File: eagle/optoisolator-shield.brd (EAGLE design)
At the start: 101.6 x 53.3 mm, 51 parts, among them Q1 MMBT2222ALT3G, Q2 MMBT2222ALT3G, Q3 MMBT2222ALT3G, Q4 MMBT2222ALT3G, Q5 MMBT2222ALT3G, Q6 MMBT2222ALT3G, U1 ILD213T, U2 ILD213T, U3 ILD213T

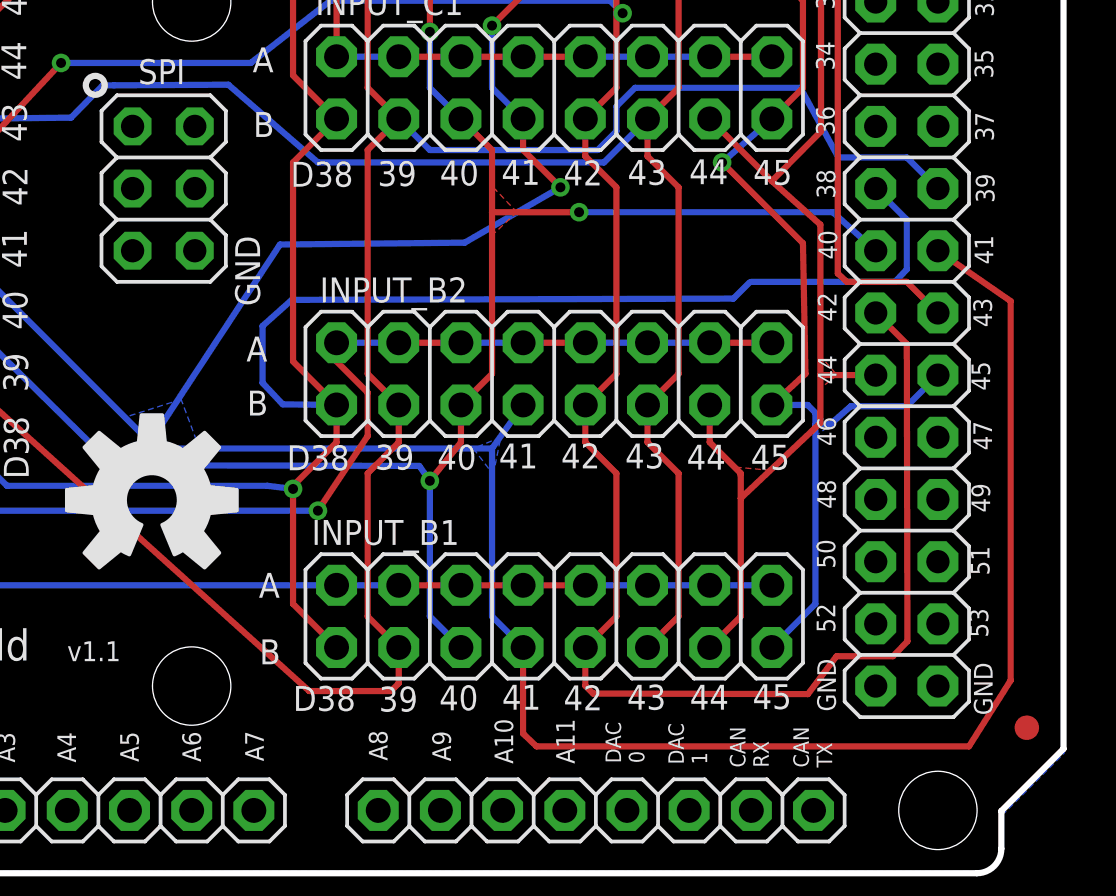
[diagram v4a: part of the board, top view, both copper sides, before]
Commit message: improved trace clearance and copper pour
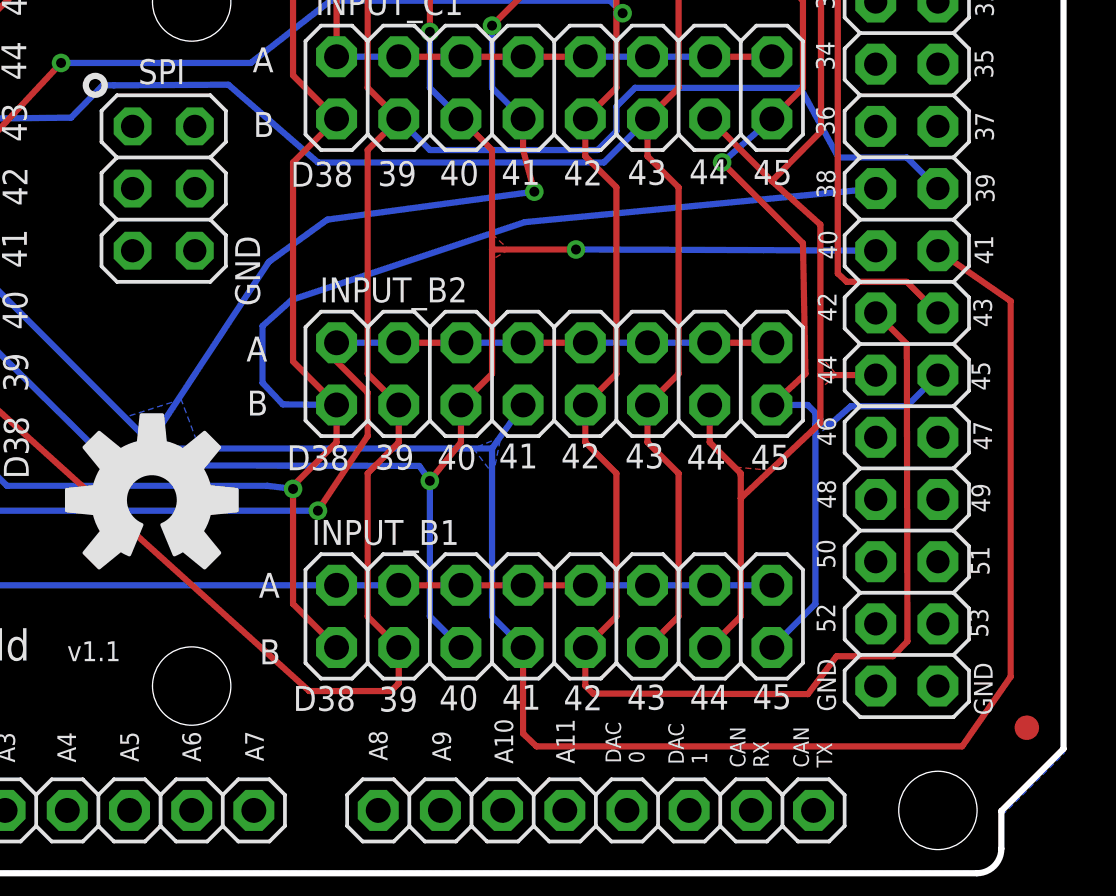
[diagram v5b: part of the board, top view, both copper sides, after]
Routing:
- net D38: track 98.5 -> 93.5 mm
- net D41: track 127.2 -> 125.2 mm
- net D40: track 83.9 -> 83.3 mm
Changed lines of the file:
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@@
 <wire x1="71.9582" y1="17.5768" x2="70.1802" y2="15.7988" width="0.254" layer="1"/>
 <wire x1="71.9582" y1="19.1008" x2="71.9582" y2="17.5768" width="0.254" layer="1"/>
-<wire x1="70.1294" y1="23.3934" x2="88.1634" y2="23.4442" width="0.254" layer="16"/>
 <wire x1="68.9356" y1="22.3266" x2="70.1294" y2="23.3934" width="0.254" layer="16"/>
 <wire x1="71.9582" y1="19.1008" x2="69.7611" y2="19.1262" width="0.254" layer="16"/>
@@
 <wire x1="71.9582" y1="19.1008" x2="70.1802" y2="20.8788" width="0.254" layer="1"/>
 <via x="70.1802" y="15.6718" extent="1-16" drill="0.4064"/>
-<wire x1="88.1634" y1="23.4442" x2="88.8238" y2="24.1046" width="0.254" layer="16"/>
-<wire x1="95.25" y1="26.67" x2="93.98" y2="27.94" width="0.254" layer="16"/>
-<wire x1="95.25" y1="24.638" x2="95.25" y2="26.67" width="0.254" layer="16"/>
-<wire x1="94.7674" y1="24.13" x2="95.25" y2="24.638" width="0.254" layer="16"/>
-<wire x1="88.9" y1="24.13" x2="94.7674" y2="24.13" width="0.254" layer="16"/>
-<wire x1="88.9" y1="24.13" x2="88.8238" y2="24.1046" width="0.1524" layer="16"/>
+<wire x1="93.98" y1="27.94" x2="79.6544" y2="26.5684" width="0.254" layer="16"/>
+<wire x1="79.6544" y1="26.5684" x2="70.1294" y2="23.3934" width="0.254" layer="16"/>
 </signal>
 <signal name="D45">
@@
 <wire x1="79.5782" y1="35.8648" x2="78.3082" y2="34.5948" width="0.254" layer="1"/>
 <wire x1="79.5782" y1="41.4528" x2="79.5782" y2="35.8648" width="0.254" layer="1"/>
-<wire x1="79.5782" y1="29.5148" x2="81.1022" y2="27.9908" width="0.254" layer="1"/>
+<wire x1="79.5782" y1="29.5148" x2="80.0354" y2="27.813" width="0.254" layer="1"/>
 <wire x1="79.5782" y1="30.7848" x2="79.5782" y2="29.5148" width="0.254" layer="1"/>
 <wire x1="48.8442" y1="26.9748" x2="47.5742" y2="25.7048" width="0.254" layer="16"/>
@@
 <wire x1="64.3382" y1="17.5768" x2="56.2102" y2="25.7048" width="0.254" layer="16"/>
 <wire x1="78.3082" y1="17.3228" x2="64.5922" y2="17.3228" width="0.254" layer="16"/>
-<wire x1="77.1906" y1="25.7302" x2="81.1022" y2="27.9908" width="0.254" layer="16"/>
-<wire x1="69.6468" y1="25.654" x2="77.1906" y2="25.7302" width="0.254" layer="16"/>
-<wire x1="64.3382" y1="17.5768" x2="69.6468" y2="25.654" width="0.254" layer="16"/>
+<wire x1="71.5772" y1="26.67" x2="80.0354" y2="27.813" width="0.254" layer="16"/>
+<wire x1="69.1896" y1="24.9428" x2="71.5772" y2="26.67" width="0.254" layer="16"/>
+<wire x1="64.3382" y1="17.5768" x2="69.1896" y2="24.9428" width="0.254" layer="16"/>
 <via x="78.3082" y="34.5948" extent="1-16" drill="0.4064"/>
-<via x="81.1022" y="27.9908" extent="1-16" drill="0.4064"/>
+<via x="80.0354" y="27.813" extent="1-16" drill="0.4064"/>
 <polygon width="0.0254" layer="16">
 <vertex x="65.6082" y="19.3294"/>
@@
 </polygon>
 <wire x1="99.4918" y1="23.3426" x2="96.52" y2="25.4" width="0.254" layer="1"/>
-<wire x1="99.4918" y1="7.8486" x2="99.4918" y2="23.3426" width="0.254" layer="1"/>
-<wire x1="97.79" y1="5.1562" x2="99.4918" y2="7.8486" width="0.254" layer="1"/>
+<wire x1="99.4918" y1="8.001" x2="99.4918" y2="23.3426" width="0.254" layer="1"/>
+<wire x1="97.5106" y1="5.1562" x2="99.4918" y2="8.001" width="0.254" layer="1"/>
 <wire x1="79.5782" y1="5.6769" x2="80.1243" y2="5.1562" width="0.254" layer="1"/>
-<wire x1="80.1243" y1="5.1562" x2="97.79" y2="5.1562" width="0.254" layer="1"/>
+<wire x1="80.1243" y1="5.1562" x2="97.5106" y2="5.1562" width="0.254" layer="1"/>
 <wire x1="79.5782" y1="5.6769" x2="79.5782" y2="9.1948" width="0.254" layer="1"/>
 </signal>
@@
 <wire x1="77.0382" y1="19.1008" x2="77.0382" y2="17.5768" width="0.254" layer="1"/>
 <wire x1="78.3082" y1="29.5148" x2="77.0382" y2="30.7848" width="0.254" layer="1"/>
-<wire x1="78.3082" y1="20.3708" x2="78.3082" y2="26.9748" width="0.254" layer="1"/>
-<wire x1="78.3082" y1="26.9748" x2="78.3082" y2="29.5148" width="0.254" layer="1"/>
+<wire x1="78.3082" y1="20.3708" x2="78.3082" y2="25.4508" width="0.254" layer="1"/>
+<wire x1="78.3082" y1="25.4508" x2="78.3082" y2="29.5148" width="0.254" layer="1"/>
 <wire x1="77.0382" y1="19.1008" x2="78.3082" y2="20.3708" width="0.254" layer="1"/>
 <wire x1="75.7682" y1="40.1828" x2="77.0382" y2="41.4528" width="0.254" layer="1"/>
 <wire x1="75.7682" y1="34.3408" x2="75.7682" y2="40.1828" width="0.254" layer="1"/>
 <wire x1="77.0382" y1="30.7848" x2="75.7682" y2="32.0548" width="0.254" layer="16"/>
-<wire x1="78.3082" y1="26.9748" x2="81.8642" y2="26.9748" width="0.254" layer="1"/>
+<wire x1="78.3082" y1="25.4508" x2="81.7372" y2="25.4508" width="0.254" layer="1"/>
 <wire x1="62.8142" y1="16.637" x2="56.2102" y2="23.1648" width="0.254" layer="16"/>
 <wire x1="75.3364" y1="16.6116" x2="62.8142" y2="16.637" width="0.254" layer="16"/>
@@
 <via x="75.7682" y="16.002" extent="1-16" drill="0.4064"/>
 <via x="75.7682" y="34.3408" extent="1-16" drill="0.4064"/>
-<via x="81.8642" y="26.9748" extent="1-16" drill="0.4064"/>
+<via x="81.7372" y="25.4508" extent="1-16" drill="0.4064"/>
+<wire x1="89.408" y1="25.4254" x2="93.98" y2="25.4" width="0.254" layer="16"/>
+<wire x1="89.408" y1="25.4254" x2="81.7372" y2="25.4508" width="0.254" layer="16"/>
+<wire x1="75.7682" y1="32.0548" x2="75.7682" y2="34.3408" width="0.254" layer="16"/>
 <polygon width="0.0254" layer="1">
-<vertex x="78.359" y="27.9908"/>
-<vertex x="79.3242" y="26.9748"/>
-<vertex x="78.2574" y="25.9842"/>
-</polygon>
-<wire x1="92.2274" y1="26.9748" x2="93.98" y2="25.4" width="0.254" layer="16"/>
-<wire x1="92.2274" y1="26.9748" x2="81.8642" y2="26.9748" width="0.254" layer="16"/>
-<wire x1="75.7682" y1="32.0548" x2="75.7682" y2="34.3408" width="0.254" layer="16"/>
+<vertex x="78.3082" y="26.0858"/>
+<vertex x="78.994" y="25.4508"/>
+<vertex x="78.2828" y="25.019"/>
+</polygon>
 </signal>
 <signal name="D39">

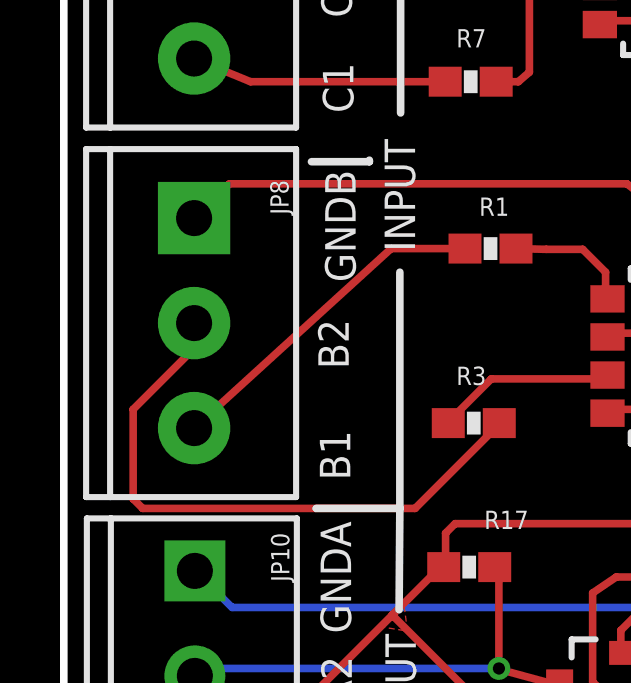
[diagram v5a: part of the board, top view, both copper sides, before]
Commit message: added shield name to schematic
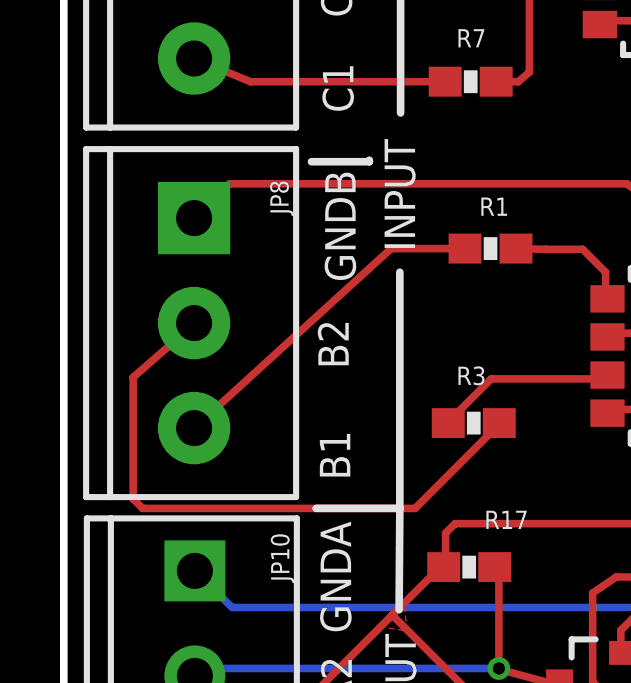
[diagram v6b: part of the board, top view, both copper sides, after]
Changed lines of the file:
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@@
 <wire x1="8.3058" y1="33.9598" x2="10.2362" y2="33.9598" width="0.254" layer="21"/>
 <wire x1="10.2362" y1="33.9598" x2="10.2362" y2="34.0106" width="0.254" layer="21"/>
-<dimension x1="101.6762" y1="37.8968" x2="0.0762" y2="37.8206" x3="50.9131375" y3="-11.392196875" textsize="1.778" layer="21" unit="inch"/>
+<dimension x1="101.6762" y1="37.8968" x2="0.0762" y2="37.8206" x3="50.9131375" y3="-11.392196875" textsize="1.778" layer="47" unit="inch"/>
 <text x="18.8214" y="48.6664" size="0.762" layer="21" font="vector" rot="R270">SCL1</text>
 <text x="21.4376" y="48.7172" size="0.762" layer="21" font="vector" rot="R270">SDA1</text>
@@
 <contactref element="JP8" pad="2"/>
 <wire x1="11.7602" y1="22.4028" x2="14.5542" y2="25.1968" width="0.254" layer="1"/>
-<wire x1="2.3622" y1="25.7048" x2="2.3622" y2="22.7203" width="0.254" layer="1"/>
+<wire x1="2.3622" y1="26.7716" x2="2.3622" y2="22.7203" width="0.254" layer="1"/>
 <wire x1="2.3622" y1="22.7203" x2="2.6797" y2="22.4028" width="0.254" layer="1"/>
 <wire x1="2.6797" y1="22.4028" x2="11.7602" y2="22.4028" width="0.254" layer="1"/>
-<wire x1="4.3942" y1="27.7368" x2="2.3622" y2="25.7048" width="0.254" layer="1"/>
-<wire x1="4.3942" y1="28.5802" x2="4.3942" y2="27.7368" width="0.254" layer="1"/>
 <wire x1="14.5542" y1="25.1968" x2="14.566" y2="25.2476" width="0.254" layer="1"/>
+<wire x1="4.3942" y1="28.5802" x2="4.572" y2="28.702" width="0.0254" layer="1"/>
+<wire x1="4.572" y1="28.702" x2="2.3622" y2="26.7716" width="0.254" layer="1"/>
 </signal>
 <signal name="IN_B1">
@@
 <wire x1="19.6342" y1="32.5882" x2="19.6342" y2="28.2448" width="0.254" layer="1"/>
 <wire x1="18.8214" y1="33.2232" x2="19.6342" y2="32.5882" width="0.254" layer="1"/>
-<wire x1="4.3942" y1="32.0802" x2="4.3942" y2="32.2453" width="0.254" layer="1"/>
-<wire x1="4.3942" y1="32.2453" x2="5.5753" y2="33.2232" width="0.254" layer="1"/>
 <wire x1="5.5753" y1="33.2232" x2="18.8214" y2="33.2232" width="0.254" layer="1"/>
 <wire x1="18.3642" y1="28.2448" x2="19.6342" y2="28.2448" width="0.254" layer="1"/>
@@
 <vertex x="19.6596" y="27.6606"/>
 </polygon>
+<wire x1="5.5753" y1="33.2232" x2="4.3942" y2="32.0802" width="0.254" layer="1"/>
 </signal>
 <signal name="EXT_VCC">
